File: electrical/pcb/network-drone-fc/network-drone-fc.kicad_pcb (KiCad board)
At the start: 4 copper layers, 36 x 36 mm, 94 parts, among them J1 U.FL-R-SMT-1, J2 TYPE-C 16PIN 2MD, J3 U.FL GPS, J4 ESC, J5 I2C port, J7 Charging board, U1 ESP32-S3FN8, U2 USBLC6-2SC6, U3 AP63205WU-7, U4 TLV75733PDBVR, U5 TPS7A2033PDBVR, U6 ICM-42688-P, U7 BMP581, U8 MAX-M10S, X1 Q22FA12800101

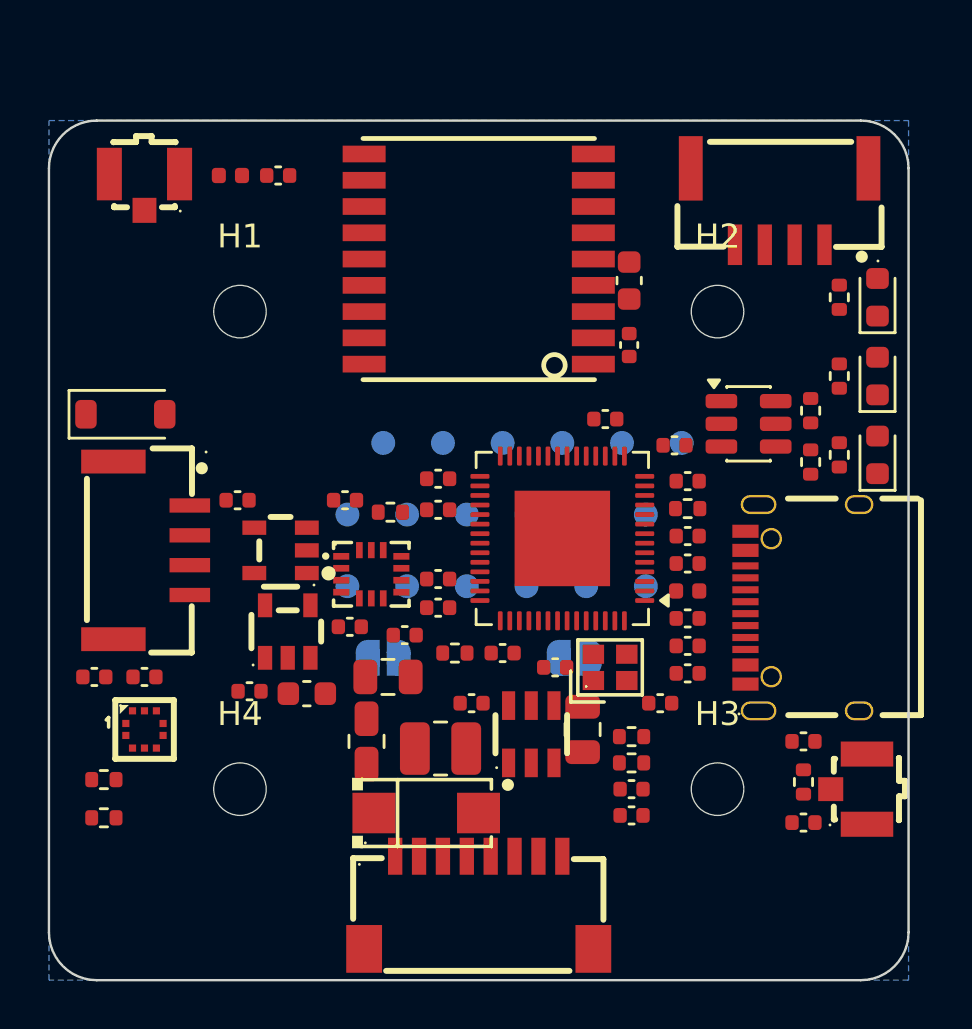
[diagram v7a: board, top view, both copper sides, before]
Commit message: PCB: 3 mm strip on top so the charging port clears the H2 grommet; every top part now 3 mm from the holes
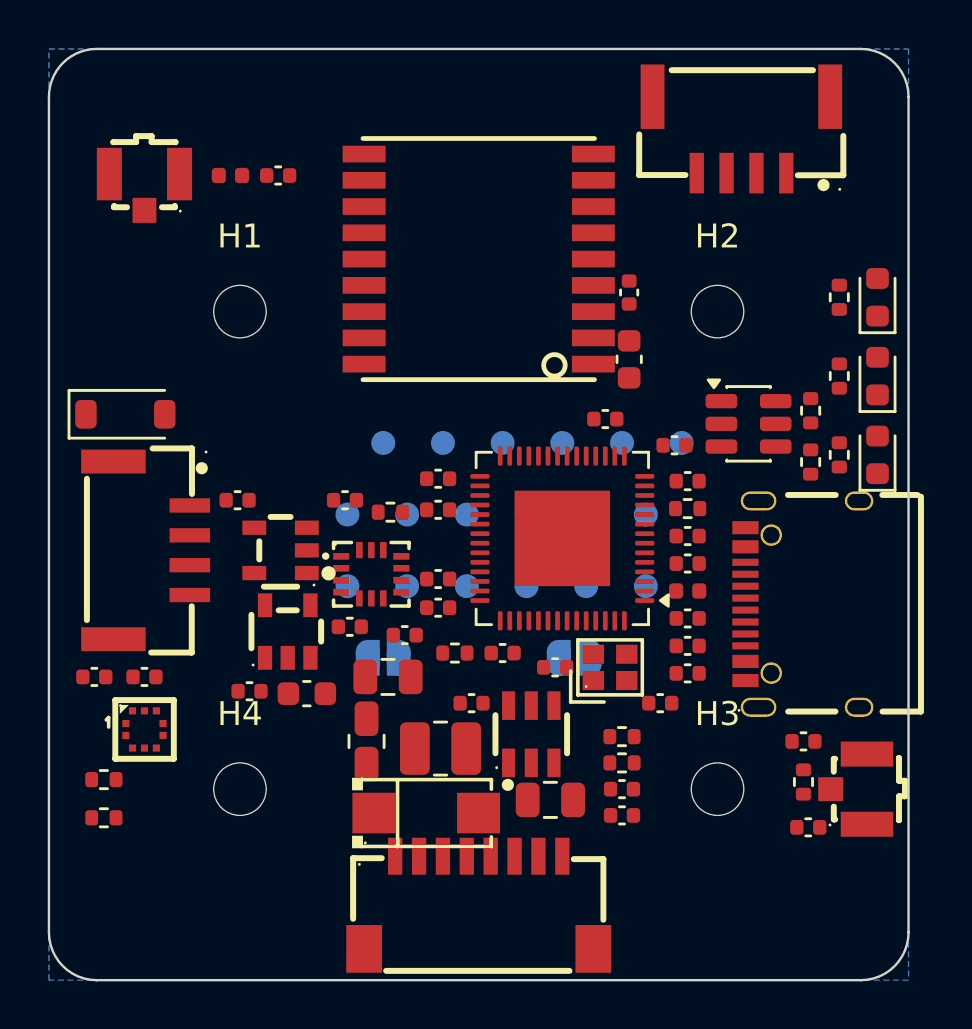
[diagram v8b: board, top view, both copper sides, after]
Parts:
- moved J7 3.40 mm to (111.0, 82.6)
- moved C30 3.30 mm to (106.3, 92.0)
- moved C16 3.24 mm to (103.0, 110.5), turned to 180 degrees
- moved C31 2.20 mm to (106.3, 89.2)
- moved C24 0.40 mm to (106.0, 110.0)
- moved C33 0.40 mm to (106.0, 111.1)
- moved R10 0.40 mm to (106.0, 108.9)
- moved R9 0.40 mm to (106.0, 107.8)
- moved C15 0.28 mm to (113.8, 111.6)
- moved J2 0.15 mm to (113.5, 102.2)
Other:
- board size 36 x 36 mm -> 36 x 39 mm
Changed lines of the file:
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@@
 	(footprint "R_0402_1005Metric"
 		(layer "F.Cu")
-		(at 106.4 107.8)
+		(at 106.0 107.8)
 		(descr "Resistor SMD 0402 (1005 Metric), square (rectangular) end terminal, IPC-7351 nominal, (Body size source: IPC-SM-782 page 72, https://www.pcb-3d.com/wordpress/wp-content/uploads/ipc-sm-782a_amendment_1_and_2.pdf), generated with kicad-footprint-generator")
 		(tags "resistor")
@@
 	(footprint "CONN-SMD_4P-P1.25_SM04B-GHS-TB-LF-SN"
 		(layer "F.Cu")
-		(at 112.6 85.6 180)
+		(at 111.0 82.6 180)
 		(property "Reference" "J7"
 			(at -0 0 180)
@@
 	(footprint "C_0402_1005Metric"
 		(layer "F.Cu")
-		(at 113.6 111.4)
+		(at 113.8 111.6)
 		(descr "Capacitor SMD 0402 (1005 Metric), square (rectangular) end terminal, IPC-7351 nominal, (Body size source: IPC-SM-782 page 76, https://www.pcb-3d.com/wordpress/wp-content/uploads/ipc-sm-782a_amendment_1_and_2.pdf), generated with kicad-footprint-generator")
 		(tags "capacitor")
@@
 	(footprint "C_0805_2012Metric"
 		(layer "F.Cu")
-		(at 104.35 107.5 90)
+		(at 103.0 110.45 180)
 		(descr "Capacitor SMD 0805 (2012 Metric), square (rectangular) end terminal, IPC-7351 nominal, (Body size source: IPC-SM-782 page 76, https://www.pcb-3d.com/wordpress/wp-content/uploads/ipc-sm-782a_amendment_1_and_2.pdf, https://docs.google.com/spreadsheets/d/1BsfQQcO9C6DZCsRaXUlFlo91Tg2WpOkGARC1WS5S8t0/edit?usp=sharing), generated with kicad-footprint-generator")
 		(tags "capacitor")
 		(property "Reference" "C16"
-			(at 0 0 90)
+			(at 0 0 180)
 			(layer "F.Fab")
 			(effects
@@
 		)
 		(property "Value" "10uF 25V"
-			(at 0 1.68 90)
+			(at 0 1.68 180)
 			(layer "F.Fab")
 			(hide yes)
@@
 		)
 		(property "Datasheet" ""
-			(at 0 0 90)
+			(at 0 0 180)
 			(layer "F.Fab")
 			(hide yes)
@@
 		)
 		(property "Description" ""
-			(at 0 0 90)
+			(at 0 0 180)
 			(layer "F.Fab")
 			(hide yes)
@@
 		)
 		(fp_text user "${REFERENCE}"
-			(at 0 0 90)
+			(at 0 0 180)
 			(layer "F.Fab")
 			(effects
@@
 		)
 		(pad "1" smd roundrect
-			(at -0.95 0 90)
+			(at -0.95 0 180)
 			(size 1 1.45)
 			(layers "F.Cu" "F.Mask" "F.Paste")
@@
 		)
 		(pad "2" smd roundrect
-			(at 0.95 0 90)
+			(at 0.95 0 180)
 			(size 1 1.45)
 			(layers "F.Cu" "F.Mask" "F.Paste")
@@
 	(footprint "C_0603_1608Metric"
 		(layer "F.Cu")
-		(at 106.3 88.7 90)
+		(at 106.3 92.0 90)
 		(descr "Capacitor SMD 0603 (1608 Metric), square (rectangular) end terminal, IPC-7351 nominal, (Body size source: IPC-SM-782 page 76, https://www.pcb-3d.com/wordpress/wp-content/uploads/ipc-sm-782a_amendment_1_and_2.pdf), generated with kicad-footprint-generator")
 		(tags "capacitor")
@@
 	(footprint "USB-C-SMD_TYPE-C-16PIN-2MD-073"
 		(layer "F.Cu")
-		(at 113.55 102.4 90)
+		(at 113.55 102.25 90)
 		(property "Reference" "J2"
 			(at 0 0 90)
@@
 	(footprint "C_0402_1005Metric"
 		(layer "F.Cu")
-		(at 106.4 111.1)
+		(at 106.0 111.1)
 		(descr "Capacitor SMD 0402 (1005 Metric), square (rectangular) end terminal, IPC-7351 nominal, (Body size source: IPC-SM-782 page 76, https://www.pcb-3d.com/wordpress/wp-content/uploads/ipc-sm-782a_amendment_1_and_2.pdf), generated with kicad-footprint-generator")
 		(tags "capacitor")
@@
 	(footprint "R_0402_1005Metric"
 		(layer "F.Cu")
-		(at 106.4 108.9)
+		(at 106.0 108.9)
 		(descr "Resistor SMD 0402 (1005 Metric), square (rectangular) end terminal, IPC-7351 nominal, (Body size source: IPC-SM-782 page 72, https://www.pcb-3d.com/wordpress/wp-content/uploads/ipc-sm-782a_amendment_1_and_2.pdf), generated with kicad-footprint-generator")
 		(tags "resistor")
@@
 	(footprint "C_0402_1005Metric"
 		(layer "F.Cu")
-		(at 106.4 110)
+		(at 106.0 110.0)
 		(descr "Capacitor SMD 0402 (1005 Metric), square (rectangular) end terminal, IPC-7351 nominal, (Body size source: IPC-SM-782 page 76, https://www.pcb-3d.com/wordpress/wp-content/uploads/ipc-sm-782a_amendment_1_and_2.pdf), generated with kicad-footprint-generator")
 		(tags "capacitor")
@@
 	(footprint "C_0402_1005Metric"
 		(layer "F.Cu")
-		(at 106.3 91.4 90)
+		(at 106.3 89.2 90)
 		(descr "Capacitor SMD 0402 (1005 Metric), square (rectangular) end terminal, IPC-7351 nominal, (Body size source: IPC-SM-782 page 76, https://www.pcb-3d.com/wordpress/wp-content/uploads/ipc-sm-782a_amendment_1_and_2.pdf), generated with kicad-footprint-generator")
 		(tags "capacitor")
@@
 	)
 	(gr_arc
-		(start 116 82)
-		(mid 117.414213 82.585786)
-		(end 118 84)
+		(start 116 79)
+		(mid 117.414213 79.585786)
+		(end 118 81)
 		(stroke
 			(width 0.1)
@@
 	)
 	(gr_line
-		(start 118 84)
+		(start 118 81)
 		(end 118 116)
 		(stroke
@@
 	)
 	(gr_arc
-		(start 82 84)
-		(mid 82.585786 82.585786)
-		(end 84 82)
+		(start 82 81)
+		(mid 82.585786 79.585786)
+		(end 84 79)
 		(stroke
 			(width 0.1)
@@
 	)
 	(gr_line
-		(start 84 82)
-		(end 116 82)
+		(start 84 79)
+		(end 116 79)
 		(stroke
 			(width 0.1)
@@
 	(gr_line
 		(start 82 116)
-		(end 82 84)
+		(end 82 81)
 		(stroke
 			(width 0.1)
@@
 		(polygon
 			(pts
-				(xy 82 82) (xy 118 82) (xy 118 118) (xy 82 118)
+				(xy 82 79) (xy 118 79) (xy 118 118) (xy 82 118)
 			)
 		)
@@
 		(polygon
 			(pts
-				(xy 82 82) (xy 118 82) (xy 118 118) (xy 82 118)
+				(xy 82 79) (xy 118 79) (xy 118 118) (xy 82 118)
 			)
 		)
